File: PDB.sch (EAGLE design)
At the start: 80 parts

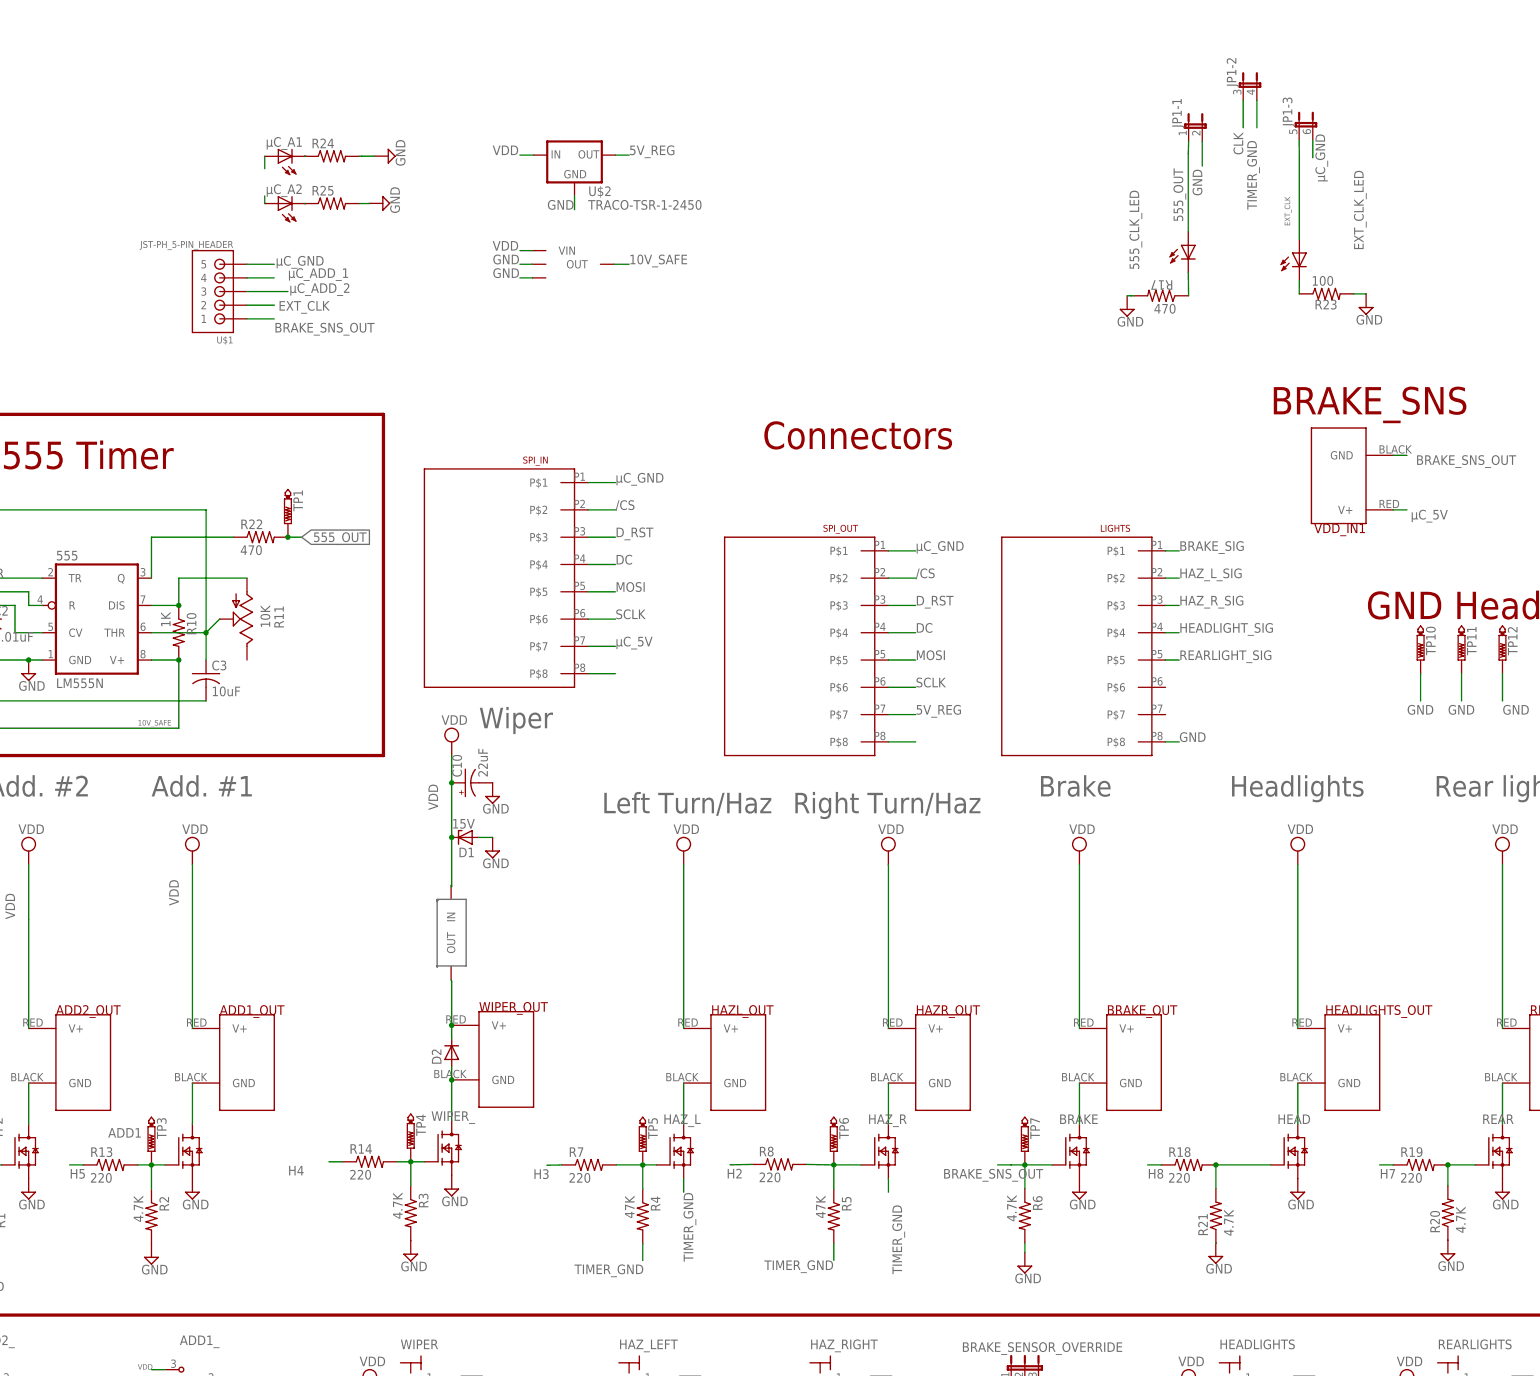
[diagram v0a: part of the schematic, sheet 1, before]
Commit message: changed grounds on LEDs to match DGND
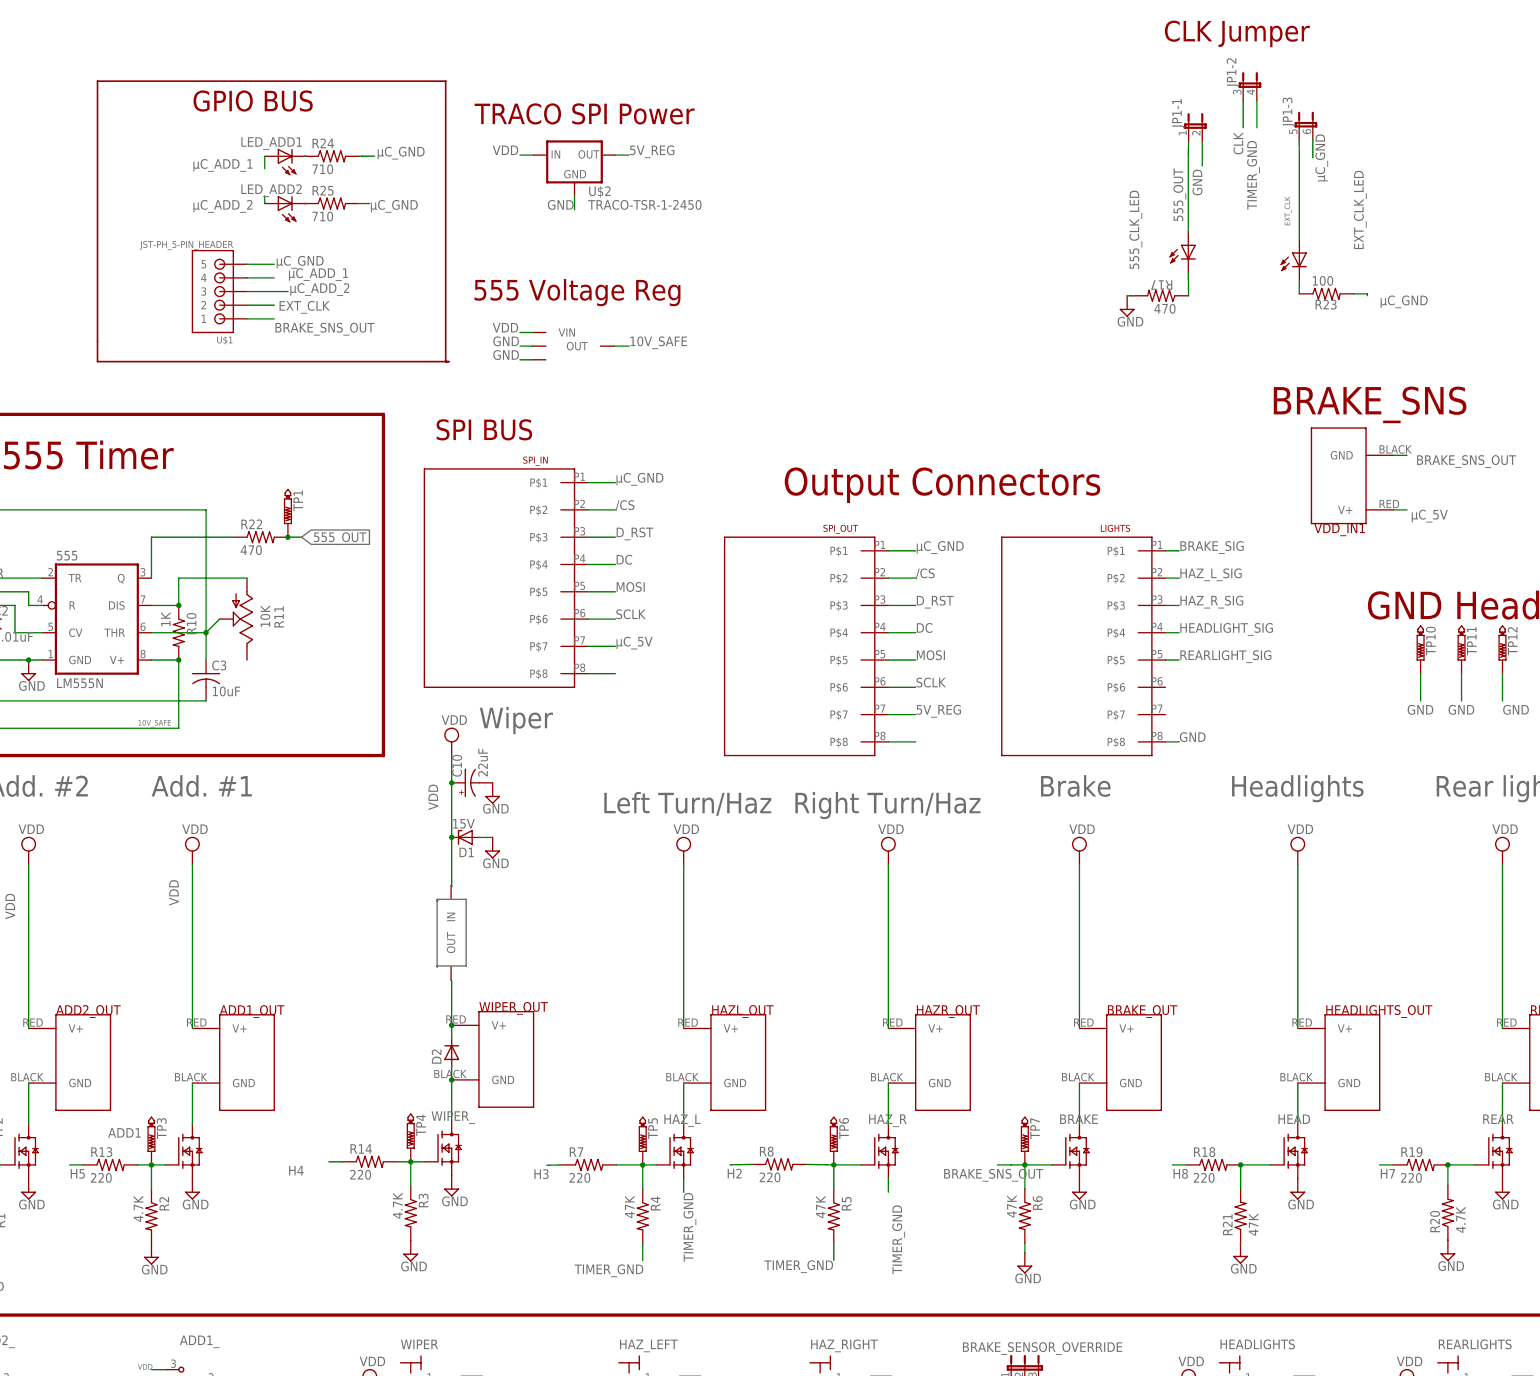
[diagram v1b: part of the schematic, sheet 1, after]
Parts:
- R21, R6: value 4.7K -> 47K
- R24, R25: value (none) -> 710
- renumbered µC_A1 to LED_ADD1, µC_A2 to LED_ADD2
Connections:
- removed net N$6: LED_ADD1.A
- removed net N$9: LED_ADD2.A
- net GND: no longer R23.2, R24.2, R25.2
- net µC_ADD_1: now also LED_ADD1.A
- net µC_ADD_2: now also LED_ADD2.A
- net µC_GND: now also R23.2, R24.2, R25.2
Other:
- note added: "555 Voltage Reg"
- note added: "CLK Jumper"
- note added: "GPIO BUS"
- note added: "Output Connectors"
- note added: "SPI BUS"
- note added: "TRACO SPI Power"
- note removed: "Connectors"
- moved on the sheet: R18, R21

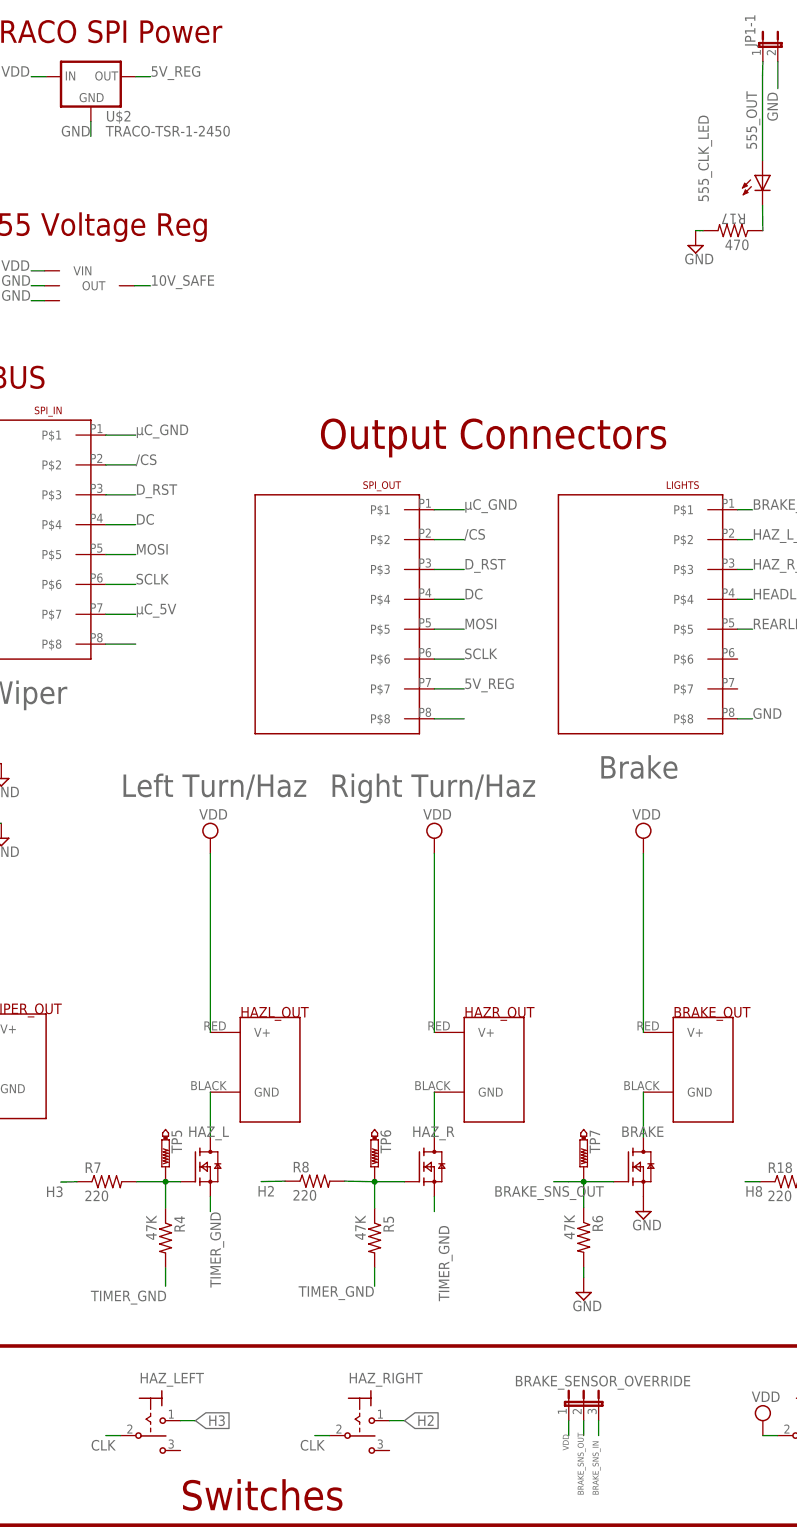
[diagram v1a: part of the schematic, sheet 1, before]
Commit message: modified PCB layout to reduce ovreall size
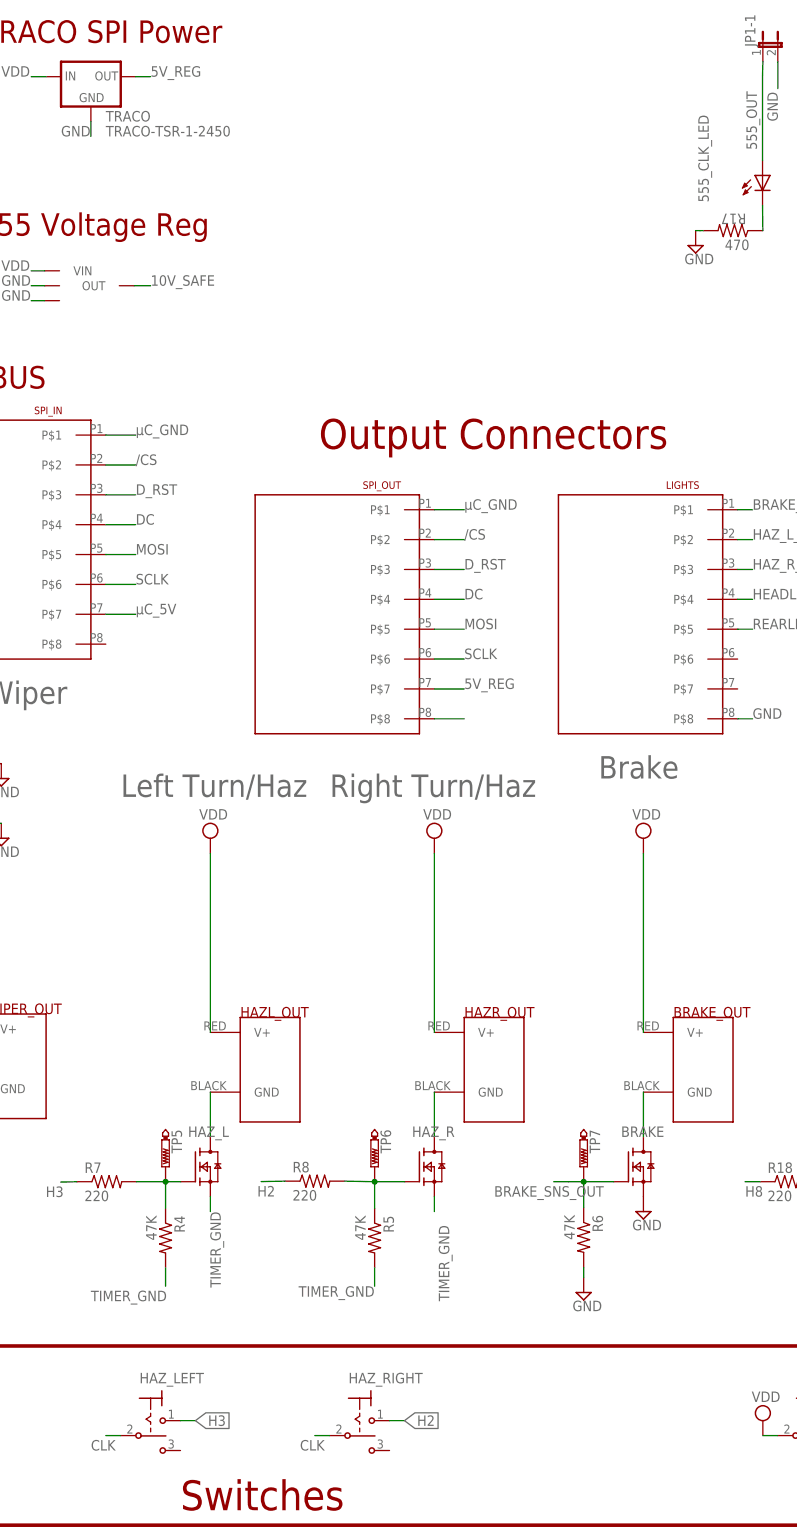
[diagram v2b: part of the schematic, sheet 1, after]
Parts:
- removed BRAKE_SENSOR_OVERRIDE: (no value), jumper:JP2E
- renumbered U$2 to TRACO, U$3 to LM2940
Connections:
- removed net BRAKE_SNS_IN: BRAKE_SENSOR_OVERRIDE.3
- removed net N$21: SPI_IN.P$8
- net BRAKE_SNS_OUT: no longer BRAKE_SENSOR_OVERRIDE.2
- net VDD: no longer BRAKE_SENSOR_OVERRIDE.1
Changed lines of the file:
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@@
 <part name="SPI_IN" library="master_library" deviceset="8-PIN-MOLEX-RA-FEMALE" device="" value="8-PIN-MOLEX-RA-FEMALE"/>
 <part name="LIGHTS" library="master_library" deviceset="8-PIN-MOLEX-RA-FEMALE" device=""/>
-<part name="BRAKE_SENSOR_OVERRIDE" library="jumper" library_urn="urn:adsk.eagle:library:252" deviceset="JP2E" device="" package3d_urn="urn:adsk.eagle:package:15452/1"/>
 <part name="POWER" library="led" library_urn="urn:adsk.eagle:library:259" deviceset="LED" device="CHIPLED_0805" package3d_urn="urn:adsk.eagle:package:15821/2"/>
 <part name="R7" library="master_library" deviceset="R-US_" device="R0805" package3d_urn="urn:adsk.eagle:package:2274104/1" value="220"/>
@@
 <part name="LED_ADD2" library="led" library_urn="urn:adsk.eagle:library:259" deviceset="LED" device="CHIPLED_0805" package3d_urn="urn:adsk.eagle:package:15821/2"/>
 <part name="U$1" library="master_library" deviceset="JST-PH_5-PIN_HEADER" device=""/>
-<part name="U$2" library="master_library" deviceset="TRACO-TSR-1-2450" device=""/>
-<part name="U$3" library="master_library" deviceset="LM2940" device="LM" package3d_urn="urn:adsk.eagle:package:8814566/1"/>
+<part name="TRACO" library="master_library" deviceset="TRACO-TSR-1-2450" device=""/>
+<part name="LM2940" library="master_library" deviceset="LM2940" device="LM" package3d_urn="urn:adsk.eagle:package:8814566/1"/>
 <part name="SPI_OUT" library="master_library" deviceset="8-PIN-MOLEX-RA-FEMALE" device="" value="8-PIN-MOLEX-RA-FEMALE"/>
 <part name="JP1" library="jumper" library_urn="urn:adsk.eagle:library:252" deviceset="JP3QE" device="" package3d_urn="urn:adsk.eagle:package:15460/1"/>
@@
 <instance part="SPI_IN" gate="G$1" x="38.1" y="119.38"/>
 <instance part="LIGHTS" gate="G$1" x="145.565" y="106.68"/>
-<instance part="BRAKE_SENSOR_OVERRIDE" gate="1" x="127" y="-33.02" smashed="yes">
-<attribute name="NAME" x="145.265" y="-27.94" size="1.778" layer="95" rot="R180"/>
-<attribute name="VALUE" x="132.715" y="-33.02" size="1.778" layer="96" rot="R90"/>
-</instance>
 <instance part="POWER" gate="G$1" x="241.3" y="144.78" smashed="yes" rot="R180">
 <attribute name="NAME" x="237.744" y="149.352" size="1.778" layer="95" rot="R270"/>
@@
 <instance part="LED_ADD2" gate="G$1" x="-11.945" y="184.02" rot="R90"/>
 <instance part="U$1" gate="G$1" x="-25.4" y="167.64" rot="R180"/>
-<instance part="U$2" gate="TSR-1-2450$1" x="43.18" y="193.04"/>
-<instance part="U$3" gate="G$1" x="42.926" y="156.21"/>
+<instance part="TRACO" gate="TSR-1-2450$1" x="43.18" y="193.04"/>
+<instance part="LM2940" gate="G$1" x="42.926" y="156.21"/>
 <instance part="SPI_OUT" gate="G$1" x="93.98" y="106.68"/>
 <instance part="JP1" gate="-1" x="157.48" y="198.12"/>
@@
 </segment>
 <segment>
-<pinref part="U$3" gate="G$1" pin="GND"/>
+<pinref part="LM2940" gate="G$1" pin="GND"/>
 <wire x1="35.306" y1="157.48" x2="33.02" y2="157.48" width="0.1524" layer="91"/>
 <label x="27.94" y="157.48" size="1.778" layer="95"/>
 </segment>
 <segment>
-<pinref part="U$3" gate="G$1" pin="GND2"/>
+<pinref part="LM2940" gate="G$1" pin="GND2"/>
 <wire x1="35.306" y1="154.94" x2="33.02" y2="154.94" width="0.1524" layer="91"/>
 <label x="27.94" y="154.94" size="1.778" layer="95"/>
 </segment>
 <segment>
-<pinref part="U$2" gate="TSR-1-2450$1" pin="GND"/>
+<pinref part="TRACO" gate="TSR-1-2450$1" pin="GND"/>
 <wire x1="43.18" y1="185.42" x2="43.18" y2="182.88" width="0.1524" layer="91"/>
 <label x="38.1" y="182.88" size="1.778" layer="95"/>
@@
 </segment>
 <segment>
-<pinref part="BRAKE_SENSOR_OVERRIDE" gate="1" pin="1"/>
-<wire x1="124.46" y1="-35.56" x2="124.46" y2="-38.1" width="0.1524" layer="91"/>
-<label x="124.46" y="-40.64" size="1.016" layer="95" rot="R90"/>
-</segment>
-<segment>
-<pinref part="U$3" gate="G$1" pin="VIN"/>
+<pinref part="LM2940" gate="G$1" pin="VIN"/>
 <wire x1="35.306" y1="160.02" x2="33.02" y2="160.02" width="0.1524" layer="91"/>
 <label x="27.94" y="160.02" size="1.778" layer="95"/>
 </segment>
 <segment>
-<pinref part="U$2" gate="TSR-1-2450$1" pin="IN"/>
+<pinref part="TRACO" gate="TSR-1-2450$1" pin="IN"/>
 <wire x1="35.56" y1="193.04" x2="33.02" y2="193.04" width="0.1524" layer="91"/>
 <label x="27.94" y="193.04" size="1.778" layer="95"/>
@@
 <wire x1="153.185" y1="99.06" x2="155.725" y2="99.06" width="0.1524" layer="91"/>
 <label x="155.725" y="99.06" size="1.778" layer="95"/>
-</segment>
-</net>
-<net name="BRAKE_SNS_IN" class="0">
-<segment>
-<pinref part="BRAKE_SENSOR_OVERRIDE" gate="1" pin="3"/>
-<wire x1="129.54" y1="-35.56" x2="129.54" y2="-38.1" width="0.1524" layer="91"/>
-<label x="129.54" y="-48.26" size="1.016" layer="95" rot="R90"/>
 </segment>
 </net>
@@
 <net name="BRAKE_SNS_OUT" class="0">
 <segment>
-<pinref part="BRAKE_SENSOR_OVERRIDE" gate="1" pin="2"/>
-<wire x1="127" y1="-35.56" x2="127" y2="-38.1" width="0.1524" layer="91"/>
-<label x="127" y="-48.26" size="1.016" layer="95" rot="R90"/>
-</segment>
-<segment>
 <wire x1="124.46" y1="5.08" x2="121.92" y2="5.08" width="0.1524" layer="91"/>
 <label x="111.76" y="2.54" size="1.778" layer="95"/>
@@
 <net name="10V_SAFE" class="0">
 <segment>
-<pinref part="U$3" gate="G$1" pin="OUT"/>
+<pinref part="LM2940" gate="G$1" pin="OUT"/>
 <wire x1="50.546" y1="157.48" x2="53.34" y2="157.48" width="0.1524" layer="91"/>
 <label x="53.34" y="157.48" size="1.778" layer="95"/>
@@
 <net name="5V_REG" class="0">
 <segment>
-<pinref part="U$2" gate="TSR-1-2450$1" pin="OUT"/>
+<pinref part="TRACO" gate="TSR-1-2450$1" pin="OUT"/>
 <wire x1="50.8" y1="193.04" x2="53.34" y2="193.04" width="0.1524" layer="91"/>
 <label x="53.34" y="193.04" size="1.778" layer="95"/>
@@
 </segment>
 </net>
-<net name="N$21" class="0">
-<segment>
-<pinref part="SPI_IN" gate="G$1" pin="P$8"/>
-<wire x1="45.72" y1="96.52" x2="50.8" y2="96.52" width="0.1524" layer="91"/>
-</segment>
-</net>

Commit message: PCB layout changes
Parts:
- added U$2: 1410-L1, master_library:1410-L1
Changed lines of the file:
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@@
 <part name="JP1" library="jumper" library_urn="urn:adsk.eagle:library:252" deviceset="JP3QE" device="" package3d_urn="urn:adsk.eagle:package:15460/1"/>
 <part name="U$4" library="master_library" deviceset="1410-L1" device=""/>
+<part name="U$2" library="master_library" deviceset="1410-L1" device=""/>
 </parts>
 <sheets>
@@
 <instance part="JP1" gate="-3" x="178.054" y="198.374"/>
 <instance part="U$4" gate="G$1" x="19.812" y="48.514" rot="R270"/>
+<instance part="U$2" gate="G$1" x="249.686" y="115.212"/>
 </instances>
 <busses>

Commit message: pcb layout
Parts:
- removed JP1: (no value), jumper:JP3QE
- removed U$2: 1410-L1, master_library:1410-L1
- added JP2: (no value), jumper:JP2E
- added JP3: (no value), jumper:JP3QE
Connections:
- new net BUCK_GND: JP3-1.1, JP3-1.2, VDD_IN.GND
- net 555_OUT: now also JP2.1; no longer JP1-1.1
- net CLK: now also JP2.2; no longer JP1-2.1
- net EXT_CLK: now also JP2.3; no longer JP1-3.1
- net GND: now also JP3-2.1, JP3-2.2, R23.2; no longer JP1-1.2, VDD_IN.GND
- net TIMER_GND: no longer JP1-2.2
- net µC_GND: now also JP3-3.1, JP3-3.2; no longer JP1-3.2, R23.2
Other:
- moved on the sheet: 555_CLK_LED, EXT_CLK_LED, LED_ADD1, LED_ADD2, LIGHTS, R17, R23, R24, R25, SPI_OUT, TRACO, U$1
